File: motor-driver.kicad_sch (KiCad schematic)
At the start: 13 parts, among them U1 L298N

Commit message: fin sch, fin placement
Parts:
- added HS1: Heatsink_Pad, heatsink:Heatsink_PI48, symbol Mechanical:Heatsink_Pad
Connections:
- net GND: now also HS1.1
- net VS: now also C1.2, D1.1 (K), D3.1 (K), D5.1 (K), D7.1 (K); no longer C2.2
- net VSS: now also C2.2; no longer C1.2, D1.1 (K), D3.1 (K), D5.1 (K), D7.1 (K)
- net M1A renamed MA1
- net M1A_IN renamed MA1_IN
- net M1B renamed MA2
- net M1B_IN renamed MA2_IN
- net M2A renamed MB1
- net M2A_IN renamed MB1_IN
- net M2B renamed MB2
- net M2B_IN renamed MB2_IN

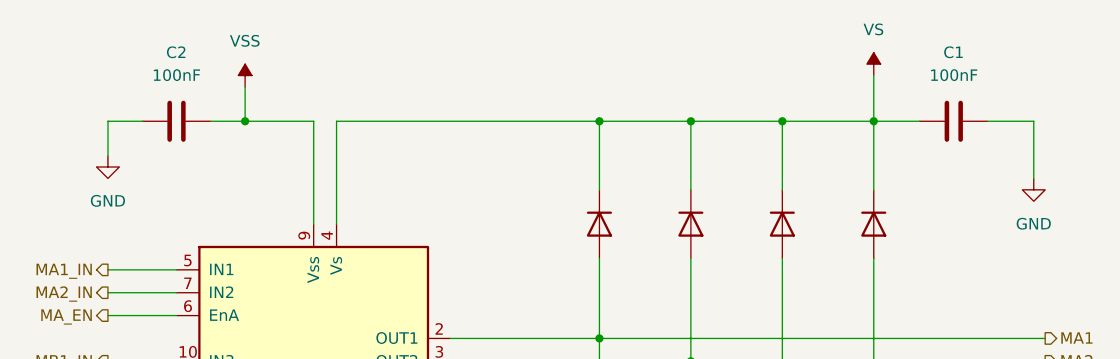
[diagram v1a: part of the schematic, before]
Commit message: placed PCB components
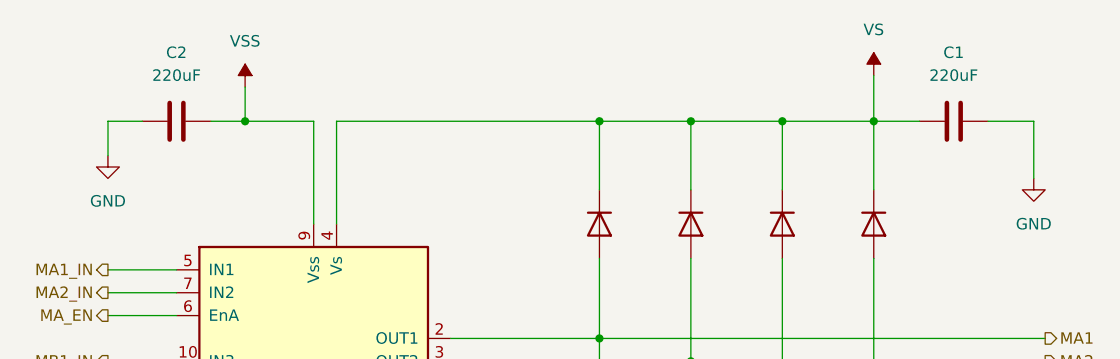
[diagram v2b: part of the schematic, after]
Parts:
- C1, C2: value 100nF -> 220uF; footprint Capacitor_THT:C_Disc_D4.7mm_W2.5mm_P5.00mm -> Capacitor_THT:C_Radial_D8.0mm_H11.5mm_P3.50mm
- D1, D2, D3, D4, D5, D6, D7, D8: footprint Diode_THT:D_DO-41_SOD81_P10.16mm_Horizontal -> Diode_SMD:D_SMA_Handsoldering
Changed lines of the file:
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@@
 			)
 		)
-		(property "Footprint" "Diode_THT:D_DO-41_SOD81_P10.16mm_Horizontal"
+		(property "Footprint" "Diode_SMD:D_SMA_Handsoldering"
 			(at 110.49 82.55 0)
 			(effects
@@
 			)
 		)
-		(property "Footprint" "Diode_THT:D_DO-41_SOD81_P10.16mm_Horizontal"
+		(property "Footprint" "Diode_SMD:D_SMA_Handsoldering"
 			(at 120.65 46.99 0)
 			(effects
@@
 			)
 		)
-		(property "Footprint" "Diode_THT:D_DO-41_SOD81_P10.16mm_Horizontal"
+		(property "Footprint" "Diode_SMD:D_SMA_Handsoldering"
 			(at 110.49 46.99 0)
 			(effects
@@
 			)
 		)
-		(property "Value" "100nF"
+		(property "Value" "220uF"
 			(at 139.7 30.48 90)
 			(effects
@@
 			)
 		)
-		(property "Footprint" "Capacitor_THT:C_Disc_D4.7mm_W2.5mm_P5.00mm"
+		(property "Footprint" "Capacitor_THT:C_Radial_D8.0mm_H11.5mm_P3.50mm"
 			(at 135.89 36.5252 0)
 			(effects
@@
 			)
 		)
-		(property "Value" "100nF"
+		(property "Value" "220uF"
 			(at 53.34 30.48 90)
 			(effects
@@
 			)
 		)
-		(property "Footprint" "Capacitor_THT:C_Disc_D4.7mm_W2.5mm_P5.00mm"
+		(property "Footprint" "Capacitor_THT:C_Radial_D8.0mm_H11.5mm_P3.50mm"
 			(at 57.15 36.5252 0)
 			(effects
@@
 			)
 		)
-		(property "Footprint" "Diode_THT:D_DO-41_SOD81_P10.16mm_Horizontal"
+		(property "Footprint" "Diode_SMD:D_SMA_Handsoldering"
 			(at 130.81 46.99 0)
 			(effects
@@
 			)
 		)
-		(property "Footprint" "Diode_THT:D_DO-41_SOD81_P10.16mm_Horizontal"
+		(property "Footprint" "Diode_SMD:D_SMA_Handsoldering"
 			(at 100.33 82.55 0)
 			(effects
@@
 			)
 		)
-		(property "Footprint" "Diode_THT:D_DO-41_SOD81_P10.16mm_Horizontal"
+		(property "Footprint" "Diode_SMD:D_SMA_Handsoldering"
 			(at 100.33 46.99 0)
 			(effects
@@
 			)
 		)
-		(property "Footprint" "Diode_THT:D_DO-41_SOD81_P10.16mm_Horizontal"
+		(property "Footprint" "Diode_SMD:D_SMA_Handsoldering"
 			(at 120.65 82.55 0)
 			(effects
@@
 			)
 		)
-		(property "Footprint" "Diode_THT:D_DO-41_SOD81_P10.16mm_Horizontal"
+		(property "Footprint" "Diode_SMD:D_SMA_Handsoldering"
 			(at 130.81 82.55 0)
 			(effects

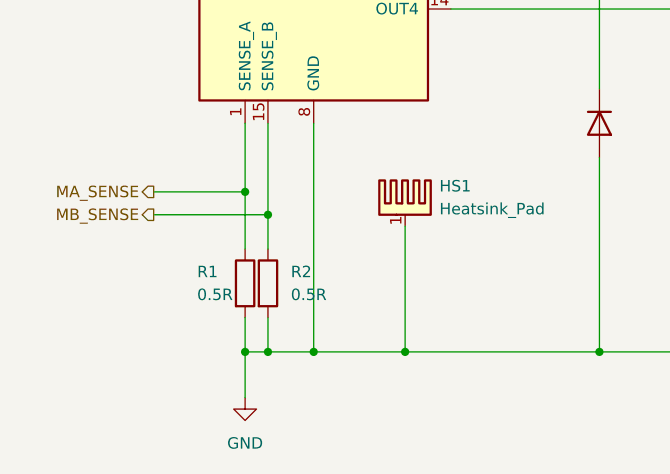
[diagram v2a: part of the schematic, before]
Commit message: set current sense resistors
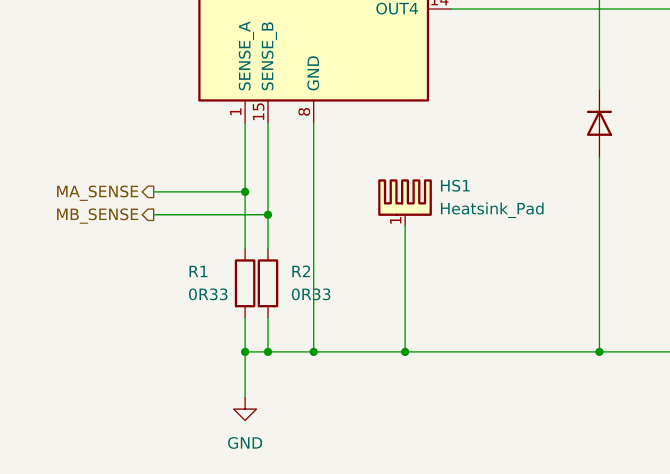
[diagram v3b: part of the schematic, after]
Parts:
- R1, R2: value 0.5R -> 0R33
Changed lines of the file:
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@@
 		(dnp no)
 		(property "Reference" "R1"
-			(at 55.626 99.06 0)
+			(at 54.61 99.06 0)
 			(effects
 				(font
@@
 			)
 		)
-		(property "Value" "0.5R"
-			(at 55.626 101.6 0)
+		(property "Value" "0R33"
+			(at 54.61 101.6 0)
 			(effects
 				(font
@@
 			)
 		)
-		(property "Value" "0.5R"
+		(property "Value" "0R33"
 			(at 66.04 101.5999 0)
 			(effects

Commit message: done placement
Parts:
- added R12, R14: 10k, Resistor_SMD:R_1206_3216Metric_Pad1.30x1.75mm_HandSolder, symbol Device:R
- added U6: 74LVC2G04, Package_TO_SOT_SMD:SOT-23-6_Handsoldering, symbol 74xGxx:74LVC2G04
- R1, R2: value 0R33 -> 0.5R
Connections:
- net GND: now also R12.2, R14.2, U6.2 (GND)
- net MA1_IN: now also U6.1
- net MA_EN: now also R12.1
- net MB1_IN: now also U6.3
- net MB_EN: now also R14.1
- net VSS: now also U6.5 (VCC)
- net MA2_IN: no longer names the net of U1.7 (IN2)
- net MA2_IN: now also U6.6
- net MB2_IN: no longer names the net of U1.12 (IN4)
- net MB2_IN: now also U6.4
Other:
- moved on the sheet: C1, C2, HS1, R1, R2

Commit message: done!?!?!
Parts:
- removed U6: 74LVC2G04, Package_TO_SOT_SMD:SOT-23-6_Handsoldering, symbol 74xGxx:74LVC2G04
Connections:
- net MB2_IN: now reaches U1.12 (IN4)
- net MA2_IN: now reaches U1.7 (IN2)
